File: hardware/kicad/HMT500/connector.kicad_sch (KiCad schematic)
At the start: 10 parts, among them J1 M_Connect_8P_Male

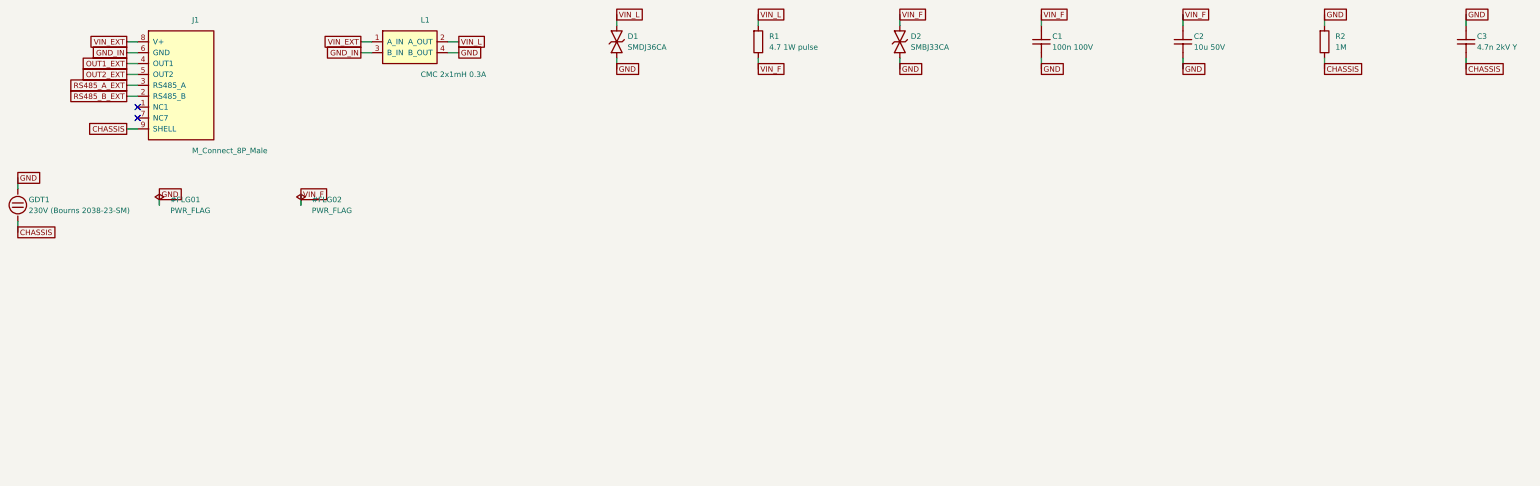
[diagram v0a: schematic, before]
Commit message: KiCad schematic v0.2: hand-laid-out, wired, readable sheets with power symbols and functional blocks
Replaces the label-only v0.1. Drawing rules are validated at generation and
the drawn netlist is checked against design intent (71 nets, 0 errors).

Co-Authored-By: Claude Opus 5.5 <noreply@anthropic.com>
Claude-Session: https://claude.ai/code/session_01JA2o8uJsqp9Vzsg4b665ev
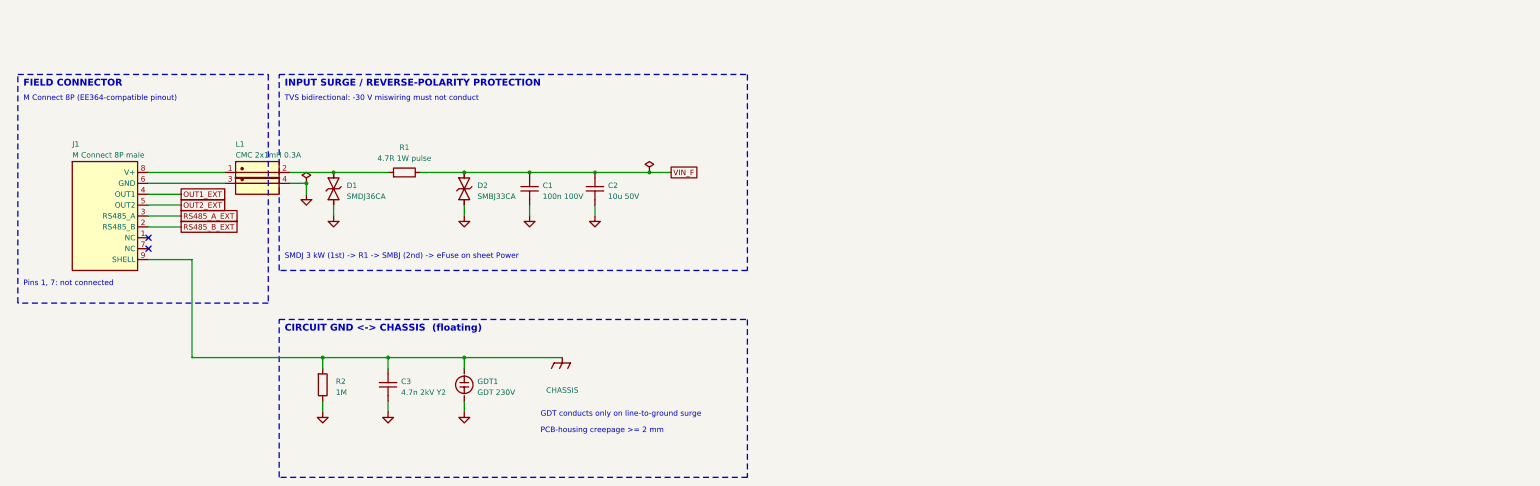
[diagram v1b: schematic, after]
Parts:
- C2: footprint Capacitor_SMD:C_1206_3216Metric -> Capacitor_SMD:C_1210_3225Metric
- C3: value 4.7n 2kV Y -> 4.7n 2kV Y2
- GDT1: value 230V (Bourns 2038-23-SM) -> GDT 230V; footprint TBD:GDT_2038 -> TBD:GDT_Bourns_2038
- J1: value M_Connect_8P_Male -> M Connect 8P male
- R1: value 4.7 1W pulse -> 4.7R 1W pulse
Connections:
- net CHASSIS: now also C3.1, GDT1.1, R2.1; no longer C3.2, GDT1.2, R2.2
- net GND: now also C3.2, GDT1.2, R2.2; no longer C3.1, GDT1.1, R2.1
- net GND_IN: no longer names the net of J1.6 (GND), L1.3
- net VIN_EXT: no longer names the net of J1.8 (V+), L1.1
- net VIN_L: no longer names the net of D1.1, L1.2, R1.1
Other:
- note added: "CIRCUIT GND <-> CHASSIS (floating)"
- note added: "FIELD CONNECTOR"
- note added: "GDT conducts only on line-to-ground surge"
- note added: "INPUT SURGE / REVERSE-POLARITY PROTECTION"
- note added: "M Connect 8P (EE364-compatible pinout)"
- note added: "PCB-housing creepage >= 2 mm"
- note added: "Pins 1, 7: not connected"
- note added: "SMDJ 3 kW (1st) -> R1 -> SMBJ (2nd) -> eFuse on sheet Power"
- note added: "TVS bidirectional: -30 V miswiring must not conduct"
- title: HMT500 - Connector, input surge protection, chassis -> HMT500  Connector & input protection
- moved on the sheet: C1, C2, C3, J1, R1, R2

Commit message: M12 field harness W-2 with JST GH 8P, epoxy-molded pass-through
- Schematic v0.5: J1 = JST GH 1.25 mm 8P side entry (SM08B-GHS-TB), pin n =
  M12 pin n; J5 chassis spring contact replaces the M12 shell pin (68 nets, 0 errors)
- Mech: J1 at PCB x 52.5-58.5 facing the connector, harness W-2 (PTFE AWG28, 60 mm)
  and plug in CAD/drawings (item 18, note 10); output-zone parts rearranged
- 7 mm pass-through filled with epoxy over its full length after the cable is in
  (item 5, primary barrier)
- Parts list, KiCad board zones, RFQ, docs, decision log #18 and tests updated

Co-Authored-By: Claude Opus 5.5 <noreply@anthropic.com>
Claude-Session: https://claude.ai/code/session_01JA2o8uJsqp9Vzsg4b665ev
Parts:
- added J5: Chassis contact, TBD:Chassis_Spring_Contact, symbol HMT500:CONN_CH
- J1: value M Connect 8P male -> SM08B-GHS-TB; footprint TBD:M_Connect_8P -> Connector_JST:JST_GH_SM08B-GHS-TB_1x08-1MP_P1.25mm_Horizontal; symbol HMT500:CONN_M8 -> HMT500:CONN_GH8
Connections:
- net CHASSIS: now also J5.1 (CHASSIS); no longer J1.9 (SHELL)
- no-connect marks 2 -> 3
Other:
- note added: "(EE364-compatible pinout, pin n = pin n)"
- note added: "J1 JST GH 8P -> harness W-2 -> M12 8P"
- note removed: "M Connect 8P (EE364-compatible pinout)"
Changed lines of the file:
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@@
 (kicad_sch (version 20230121) (generator eeschema) (paper "A4")
-(title_block (title "HMT500  Connector & input protection") (date "2026-09-29") (rev "0.4") (company "DOTECH Co., Ltd.") (comment 1 "Oil moisture transmitter HMT500 - RS-485 + 2x V/I analog output") (comment 2 "Design notes: docs/hw/circuit-design.md") (comment 3 "VERIFY=YES parts: pin numbers LMR36006/PCAP04/DAC8760/TPS26611; TPS2660 R22"))
-(symbol (lib_id "HMT500:CONN_M8") (at 45.72 81.28 0) (unit 1) (in_bom yes) (on_board yes) (dnp no) (property "Reference" "J1" (at 38.1 64.516 0) (effects (font (size 1.27 1.27)) (justify left))) (property "Value" "M Connect 8P male" (at 38.1 67.056 0) (effects (font (size 1.27 1.27)) (justify left))) (property "Footprint" "TBD:M_Connect_8P" (at 45.72 81.28 0) (effects (font (size 1.27 1.27)) hide)) (property "Datasheet" "~" (at 45.72 81.28 0) (effects (font (size 1.27 1.27)) hide)) (pin "8") (pin "6") (pin "4") (pin "5") (pin "3") (pin "2") (pin "1") (pin "7") (pin "9") (instances (project "HMT500" (path "/1ebb025b-11bd-5f7c-aaab-41e2a750e8b3/d8924d4b-0329-5e79-8dd6-1c12c7722a4b" (reference "J1") (unit 1)))))
+(title_block (title "HMT500  Connector & input protection") (date "2026-09-29") (rev "0.5") (company "DOTECH Co., Ltd.") (comment 1 "Oil moisture transmitter HMT500 - RS-485 + 2x V/I analog output") (comment 2 "Design notes: docs/hw/circuit-design.md") (comment 3 "VERIFY=YES parts: pin numbers LMR36006/PCAP04/DAC8760/TPS26611; TPS2660 R22"))
+(symbol (lib_id "HMT500:CONN_GH8") (at 45.72 81.28 0) (unit 1) (in_bom yes) (on_board yes) (dnp no) (property "Reference" "J1" (at 38.1 64.516 0) (effects (font (size 1.27 1.27)) (justify left))) (property "Value" "SM08B-GHS-TB" (at 38.1 67.056 0) (effects (font (size 1.27 1.27)) (justify left))) (property "Footprint" "Connector_JST:JST_GH_SM08B-GHS-TB_1x08-1MP_P1.25mm_Horizontal" (at 45.72 81.28 0) (effects (font (size 1.27 1.27)) hide)) (property "Datasheet" "~" (at 45.72 81.28 0) (effects (font (size 1.27 1.27)) hide)) (pin "8") (pin "6") (pin "4") (pin "5") (pin "3") (pin "2") (pin "1") (pin "7") (pin "MP") (instances (project "HMT500" (path "/1ebb025b-11bd-5f7c-aaab-41e2a750e8b3/d8924d4b-0329-5e79-8dd6-1c12c7722a4b" (reference "J1") (unit 1)))))
 (symbol (lib_id "HMT500:CMC") (at 81.28 71.12 0) (unit 1) (in_bom yes) (on_board yes) (dnp no) (property "Reference" "L1" (at 76.2 64.516 0) (effects (font (size 1.27 1.27)) (justify left))) (property "Value" "CMC 2x1mH 0.3A" (at 76.2 67.056 0) (effects (font (size 1.27 1.27)) (justify left))) (property "Footprint" "TBD:CMC_WE-SL" (at 81.28 71.12 0) (effects (font (size 1.27 1.27)) hide)) (property "Datasheet" "~" (at 81.28 71.12 0) (effects (font (size 1.27 1.27)) hide)) (pin "1") (pin "3") (pin "2") (pin "4") (instances (project "HMT500" (path "/1ebb025b-11bd-5f7c-aaab-41e2a750e8b3/d8924d4b-0329-5e79-8dd6-1c12c7722a4b" (reference "L1") (unit 1)))))
 (symbol (lib_id "HMT500:PWR_FLAG") (at 92.71 73.66 0) (unit 1) (in_bom no) (on_board no) (dnp no) (property "Reference" "#FLG001" (at 92.71 65.532 0) (effects (font (size 1.27 1.27)) hide)) (property "Value" "PWR_FLAG" (at 92.71 67.818 0) (effects (font (size 1.27 1.27)) hide)) (property "Footprint" "" (at 92.71 73.66 0) (effects (font (size 1.27 1.27)) hide)) (property "Datasheet" "~" (at 92.71 73.66 0) (effects (font (size 1.27 1.27)) hide)) (pin "1") (instances (project "HMT500" (path "/1ebb025b-11bd-5f7c-aaab-41e2a750e8b3/d8924d4b-0329-5e79-8dd6-1c12c7722a4b" (reference "#FLG001") (unit 1)))))
@@
 (symbol (lib_id "HMT500:GND") (at 160.02 81.28 0) (unit 1) (in_bom no) (on_board no) (dnp no) (property "Reference" "#PWR006" (at 160.02 87.63 0) (effects (font (size 1.27 1.27)) hide)) (property "Value" "GND" (at 160.02 88.9 0) (effects (font (size 1.27 1.27)) hide)) (property "Footprint" "" (at 160.02 81.28 0) (effects (font (size 1.27 1.27)) hide)) (property "Datasheet" "~" (at 160.02 81.28 0) (effects (font (size 1.27 1.27)) hide)) (pin "1") (instances (project "HMT500" (path "/1ebb025b-11bd-5f7c-aaab-41e2a750e8b3/d8924d4b-0329-5e79-8dd6-1c12c7722a4b" (reference "#PWR006") (unit 1)))))
 (symbol (lib_id "HMT500:PWR_FLAG") (at 172.72 71.12 0) (unit 1) (in_bom no) (on_board no) (dnp no) (property "Reference" "#FLG007" (at 172.72 62.992 0) (effects (font (size 1.27 1.27)) hide)) (property "Value" "PWR_FLAG" (at 172.72 65.278 0) (effects (font (size 1.27 1.27)) hide)) (property "Footprint" "" (at 172.72 71.12 0) (effects (font (size 1.27 1.27)) hide)) (property "Datasheet" "~" (at 172.72 71.12 0) (effects (font (size 1.27 1.27)) hide)) (pin "1") (instances (project "HMT500" (path "/1ebb025b-11bd-5f7c-aaab-41e2a750e8b3/d8924d4b-0329-5e79-8dd6-1c12c7722a4b" (reference "#FLG007") (unit 1)))))
+(symbol (lib_id "HMT500:CONN_CH") (at 45.72 119.38 0) (unit 1) (in_bom yes) (on_board yes) (dnp no) (property "Reference" "J5" (at 38.1 112.776 0) (effects (font (size 1.27 1.27)) (justify left))) (property "Value" "Chassis contact" (at 38.1 115.316 0) (effects (font (size 1.27 1.27)) (justify left))) (property "Footprint" "TBD:Chassis_Spring_Contact" (at 45.72 119.38 0) (effects (font (size 1.27 1.27)) hide)) (property "Datasheet" "~" (at 45.72 119.38 0) (effects (font (size 1.27 1.27)) hide)) (pin "1") (instances (project "HMT500" (path "/1ebb025b-11bd-5f7c-aaab-41e2a750e8b3/d8924d4b-0329-5e79-8dd6-1c12c7722a4b" (reference "J5") (unit 1)))))
 (symbol (lib_id "HMT500:R") (at 96.52 120.65 0) (unit 1) (in_bom yes) (on_board yes) (dnp no) (property "Reference" "R2" (at 99.568 119.888 0) (effects (font (size 1.27 1.27)) (justify left))) (property "Value" "1M" (at 99.568 122.428 0) (effects (font (size 1.27 1.27)) (justify left))) (property "Footprint" "Resistor_SMD:R_0603_1608Metric" (at 96.52 120.65 0) (effects (font (size 1.27 1.27)) hide)) (property "Datasheet" "~" (at 96.52 120.65 0) (effects (font (size 1.27 1.27)) hide)) (pin "1") (pin "2") (instances (project "HMT500" (path "/1ebb025b-11bd-5f7c-aaab-41e2a750e8b3/d8924d4b-0329-5e79-8dd6-1c12c7722a4b" (reference "R2") (unit 1)))))
 (symbol (lib_id "HMT500:C") (at 111.76 120.65 0) (unit 1) (in_bom yes) (on_board yes) (dnp no) (property "Reference" "C3" (at 114.808 119.888 0) (effects (font (size 1.27 1.27)) (justify left))) (property "Value" "4.7n 2kV Y2" (at 114.808 122.428 0) (effects (font (size 1.27 1.27)) (justify left))) (property "Footprint" "Capacitor_SMD:C_1812_4532Metric" (at 111.76 120.65 0) (effects (font (size 1.27 1.27)) hide)) (property "Datasheet" "~" (at 111.76 120.65 0) (effects (font (size 1.27 1.27)) hide)) (pin "1") (pin "2") (instances (project "HMT500" (path "/1ebb025b-11bd-5f7c-aaab-41e2a750e8b3/d8924d4b-0329-5e79-8dd6-1c12c7722a4b" (reference "C3") (unit 1)))))
@@
 (wire (pts (xy 55.88 81.28) (xy 63.5 81.28)) (stroke (width 0) (type default)))
 (wire (pts (xy 55.88 83.82) (xy 63.5 83.82)) (stroke (width 0) (type default)))
-(wire (pts (xy 55.88 91.44) (xy 66.04 91.44)) (stroke (width 0) (type default)))
-(wire (pts (xy 66.04 91.44) (xy 66.04 114.3)) (stroke (width 0) (type default)))
+(wire (pts (xy 55.88 119.38) (xy 66.04 119.38)) (stroke (width 0) (type default)))
+(wire (pts (xy 66.04 119.38) (xy 66.04 114.3)) (stroke (width 0) (type default)))
 (wire (pts (xy 66.04 114.3) (xy 96.52 114.3)) (stroke (width 0) (type default)))
 (wire (pts (xy 96.52 114.3) (xy 111.76 114.3)) (stroke (width 0) (type default)))
@@
 (no_connect (at 55.88 86.36))
 (no_connect (at 55.88 88.9))
+(no_connect (at 55.88 91.44))
 (junction (at 92.71 73.66) (diameter 0) (color 0 0 0 0))
 (junction (at 96.52 114.3) (diameter 0) (color 0 0 0 0))
@@
 (rectangle (start 86.36 105.41) (end 195.58 142.24) (stroke (width 0.1524) (type dash) (color 72 72 160 1)) (fill (type none)))
 (text "FIELD CONNECTOR" (at 26.67 51.308 0) (effects (font (size 1.6 1.6) bold) (justify left bottom)))
-(text "M Connect 8P (EE364-compatible pinout)" (at 26.67 54.61 0) (effects (font (size 1.27 1.27)) (justify left bottom)))
+(text "J1 JST GH 8P -> harness W-2 -> M12 8P" (at 26.67 54.61 0) (effects (font (size 1.27 1.27)) (justify left bottom)))
+(text "(EE364-compatible pinout, pin n = pin n)" (at 26.67 58.42 0) (effects (font (size 1.27 1.27)) (justify left bottom)))
 (text "Pins 1, 7: not connected" (at 26.67 97.79 0) (effects (font (size 1.27 1.27)) (justify left bottom)))
 (text "INPUT SURGE / REVERSE-POLARITY PROTECTION" (at 87.63 51.308 0) (effects (font (size 1.6 1.6) bold) (justify left bottom)))

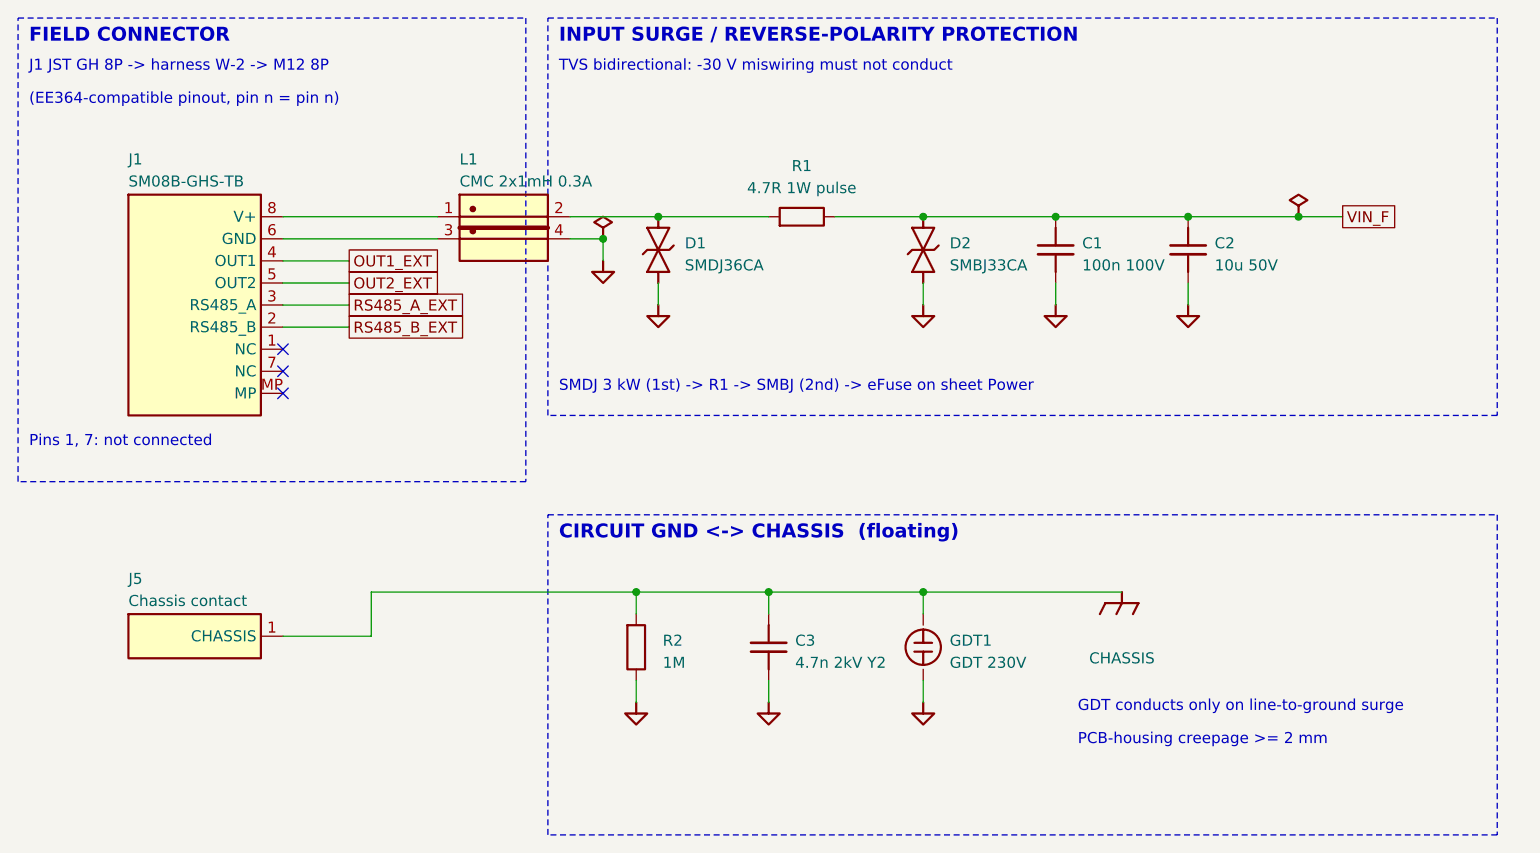
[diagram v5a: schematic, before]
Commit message: Schematic drawing rules: no overlapping text, Korean font, distinct net names
- Generator places reference/value text automatically, clear of symbol bodies,
  pins, wires, labels, notes and box edges; validation fails on any overlap
  (also note text vs wires/power names and bodies vs box edges)
- Fix 180-degree parts (LED) whose justification KiCad mirrors
- Styles: reference bold, value normal, power nets italic, signal nets boxed labels
- Korean box subtitles and legend in NanumGothic TrueType (stroke font has no Hangul)
- Nets renamed where they matched part or pin names: LED -> STAT_LED, EF_ILIM/IMON/DVDT
- J1 GH mounting pads removed from the symbol (PCB only); connector sheet re-spaced
- Schematic PDF export added; tests for net naming and Hangul font

Co-Authored-By: Claude Opus 5.5 <noreply@anthropic.com>
Claude-Session: https://claude.ai/code/session_01JA2o8uJsqp9Vzsg4b665ev
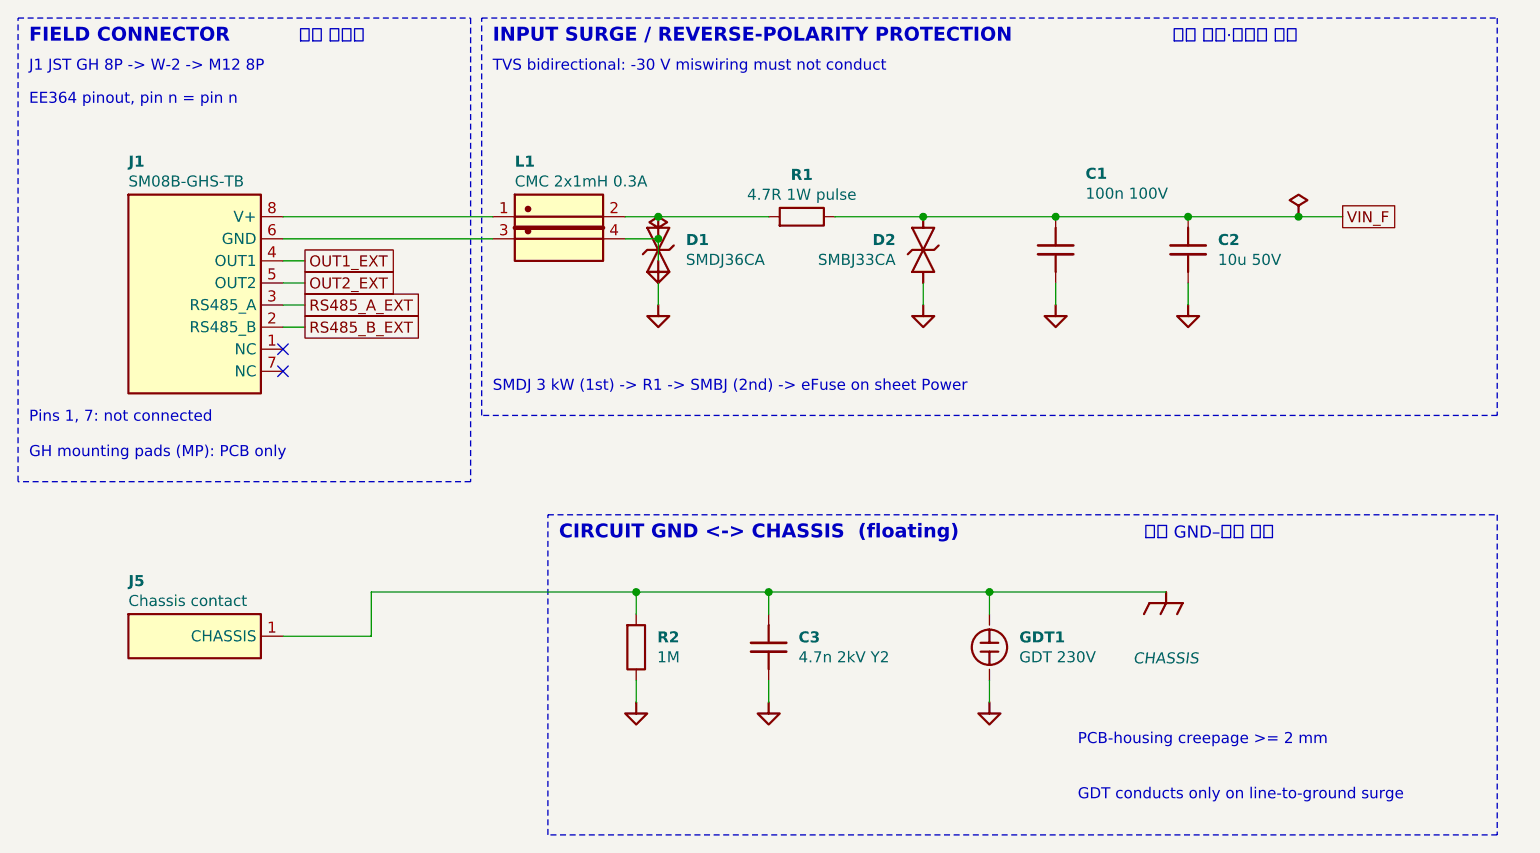
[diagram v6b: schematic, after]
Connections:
- no-connect marks 3 -> 2
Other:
- note added: "EE364 pinout, pin n = pin n"
- note added: "GH mounting pads (MP): PCB only"
- note added: "J1 JST GH 8P -> W-2 -> M12 8P"
- note added: "입력 서지·역극성 보호"
- note added: "현장 커넥터"
- note added: "회로 GND–외함 분리"
- note removed: "(EE364-compatible pinout, pin n = pin n)"
- note removed: "J1 JST GH 8P -> harness W-2 -> M12 8P"
- moved on the sheet: GDT1, L1

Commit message: Schematic v0.6: parts cleanup (91 -> 75) and PCB temperature sensing
- Removed: fault pull-ups R11-R15 (MCU internal pull-ups), status LED D3/R16
  (not visible after potting), RS-485 R60/R61/D60/D61 (THVD2450 built-in
  protection), VREF+ filter FB2/C19 (MCU ADC only for diagnostics), C11/C2/C6
  (duplicated by adjacent capacitors); VREF+ tied to +3V3 with C20
- PCB temperature with no added parts: ADS1220 internal sensor at the measurement
  front, STM32G0 internal sensor mid-board; compensation plan in circuit-design 5B
- 63 nets, netlist check 0 errors; parts list regenerated; decision log #22/#23

Co-Authored-By: Claude Opus 5.5 <noreply@anthropic.com>
Claude-Session: https://claude.ai/code/session_01JA2o8uJsqp9Vzsg4b665ev
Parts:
- removed C2: 10u 50V, Capacitor_SMD:C_1210_3225Metric, symbol HMT500:C
